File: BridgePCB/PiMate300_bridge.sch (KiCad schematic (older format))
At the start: 28 parts, among them J1 PI_CON, J2 LEFT_CON, J3 RIGHT_CON, U1 KBD_ROW, U2 CD74HC4067SM, U3 KBD_COL

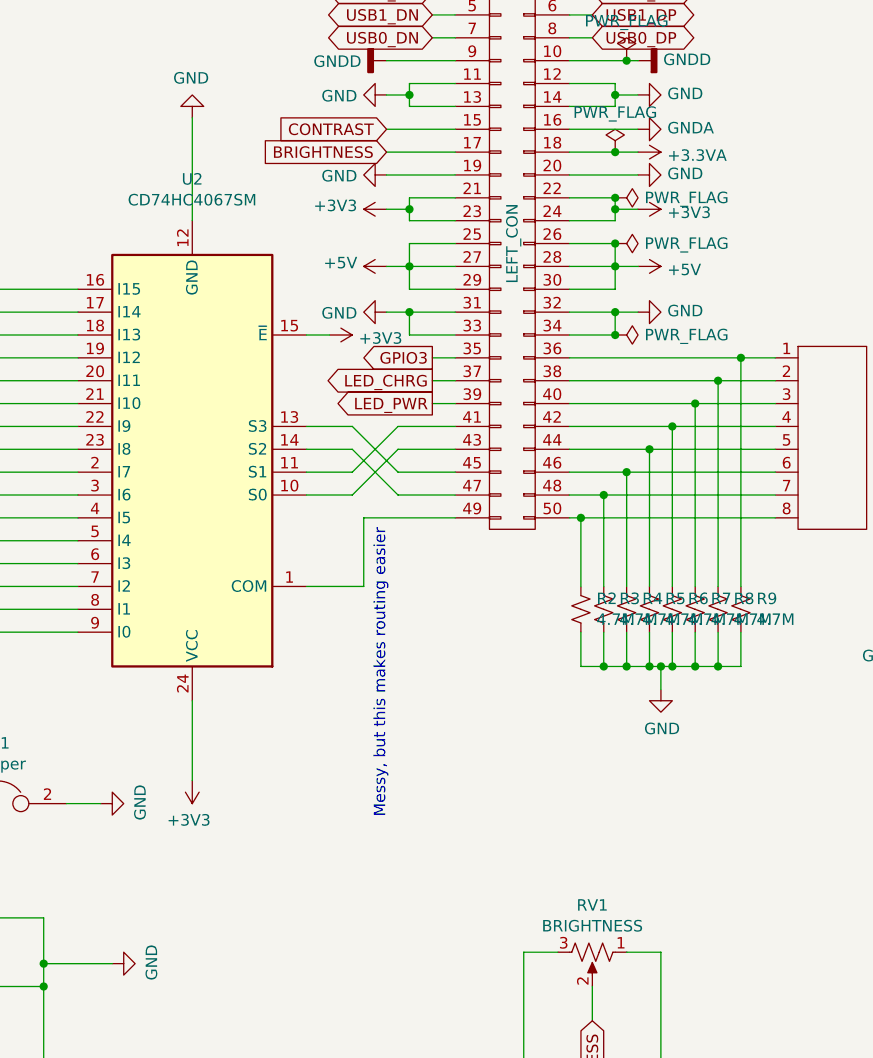
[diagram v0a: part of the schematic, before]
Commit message: Started work on Right PCB, added model for double stack USB and started positioning.
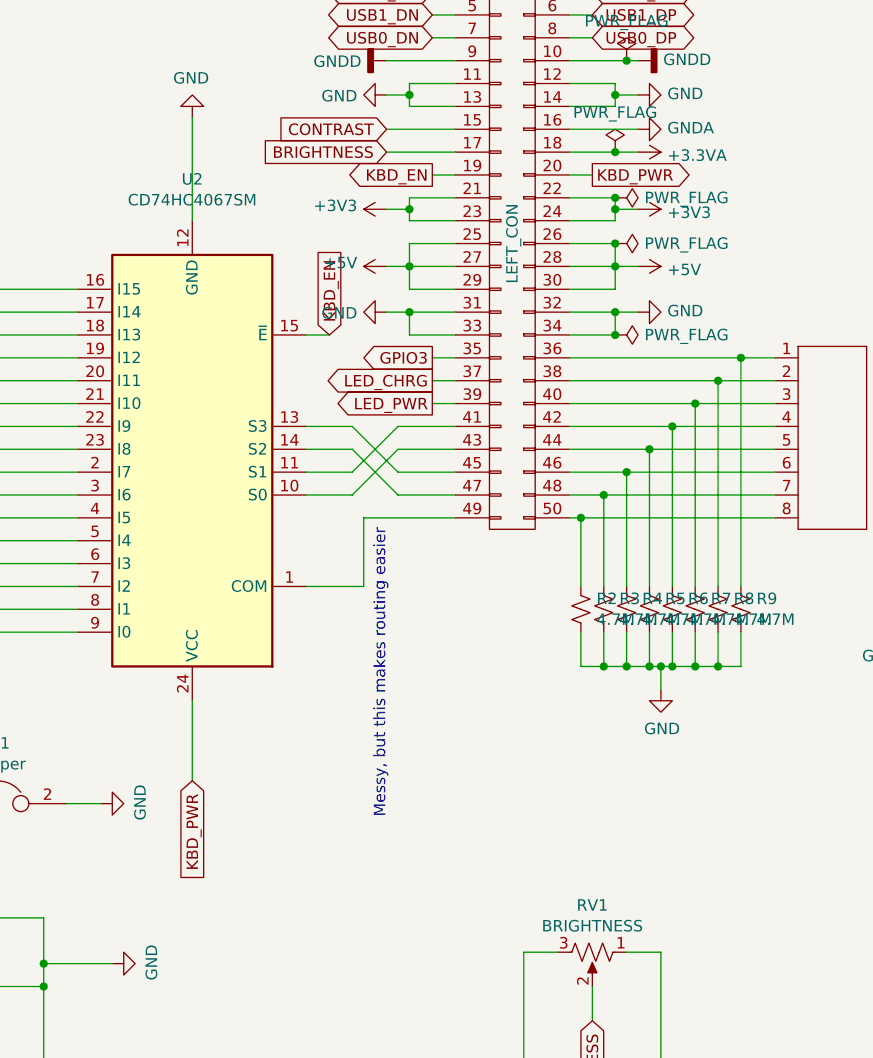
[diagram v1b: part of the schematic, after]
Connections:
- net +3V3: no longer U2.15 (~E), U2.24 (VCC)
- net GND: no longer J2.19 (P19), J2.20 (P20)
- new net KBD_EN: J2.19 (P19), U2.15 (~E)
- new net KBD_PWR: J2.20 (P20), U2.24 (VCC)
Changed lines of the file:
@@
 Connection ~ 7800 4500
-$Comp
-L power:+3V3 #PWR0112
-U 1 1 5E529646
-P 3900 4700
-F 0 "#PWR0112" H 3900 4550 50  0001 C CNN
-F 1 "+3V3" H 3915 4873 50  0000 C CNN
-F 2 "" H 3900 4700 50  0001 C CNN
-F 3 "" H 3900 4700 50  0001 C CNN
-	1    3900 4700
-	-1   0    0    1
-$EndComp
 $Comp
 L power:GND #PWR0113
@@
 	1    3900 1800
 	-1   0    0    1
-$EndComp
-$Comp
-L power:+3V3 #PWR0114
-U 1 1 5E52E51D
-P 4500 2750
-F 0 "#PWR0114" H 4500 2600 50  0001 C CNN
-F 1 "+3V3" V 4515 2878 50  0000 L CNN
-F 2 "" H 4500 2750 50  0001 C CNN
-F 3 "" H 4500 2750 50  0001 C CNN
-	1    4500 2750
-	0    1    1    0
 $EndComp
 Wire Wire Line
@@
 	5750 2250 5750 2200
 Connection ~ 5750 2200
-$Comp
-L power:GND #PWR0133
-U 1 1 5EBBD187
-P 5850 2050
-F 0 "#PWR0133" H 5850 1800 50  0001 C CNN
-F 1 "GND" V 5855 1922 50  0000 R CNN
-F 2 "" H 5850 2050 50  0001 C CNN
-F 3 "" H 5850 2050 50  0001 C CNN
-	1    5850 2050
-	0    -1   -1   0
-$EndComp
-$Comp
-L power:GND #PWR0134
-U 1 1 5EBBD57C
-P 4750 2050
-F 0 "#PWR0134" H 4750 1800 50  0001 C CNN
-F 1 "GND" V 4755 1922 50  0000 R CNN
-F 2 "" H 4750 2050 50  0001 C CNN
-F 3 "" H 4750 2050 50  0001 C CNN
-	1    4750 2050
-	0    1    1    0
-$EndComp
-Wire Wire Line
-	4750 2050 5050 2050
-Wire Wire Line
-	5550 2050 5850 2050
 Wire Wire Line
 	5850 1950 5750 1950
@@
 Wire Wire Line
 	2750 4800 2600 4800
+Wire Wire Line
+	4950 2050 5050 2050
+Wire Wire Line
+	5650 2050 5550 2050
+Text GLabel 4950 2050 0    50   Output ~ 0
+KBD_EN
+Text GLabel 5650 2050 2    50   Output ~ 0
+KBD_PWR
+Text GLabel 3900 4700 3    50   Input ~ 0
+KBD_PWR
+Text GLabel 4500 2750 1    50   Input ~ 0
+KBD_EN
 $EndSCHEMATC
